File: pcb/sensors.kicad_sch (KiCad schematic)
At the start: 6 parts, among them U3 INA230AIRGTT, U4 MCP9804_DFN, U6 INA230AIRGTT, U7 INA230AIRGTT

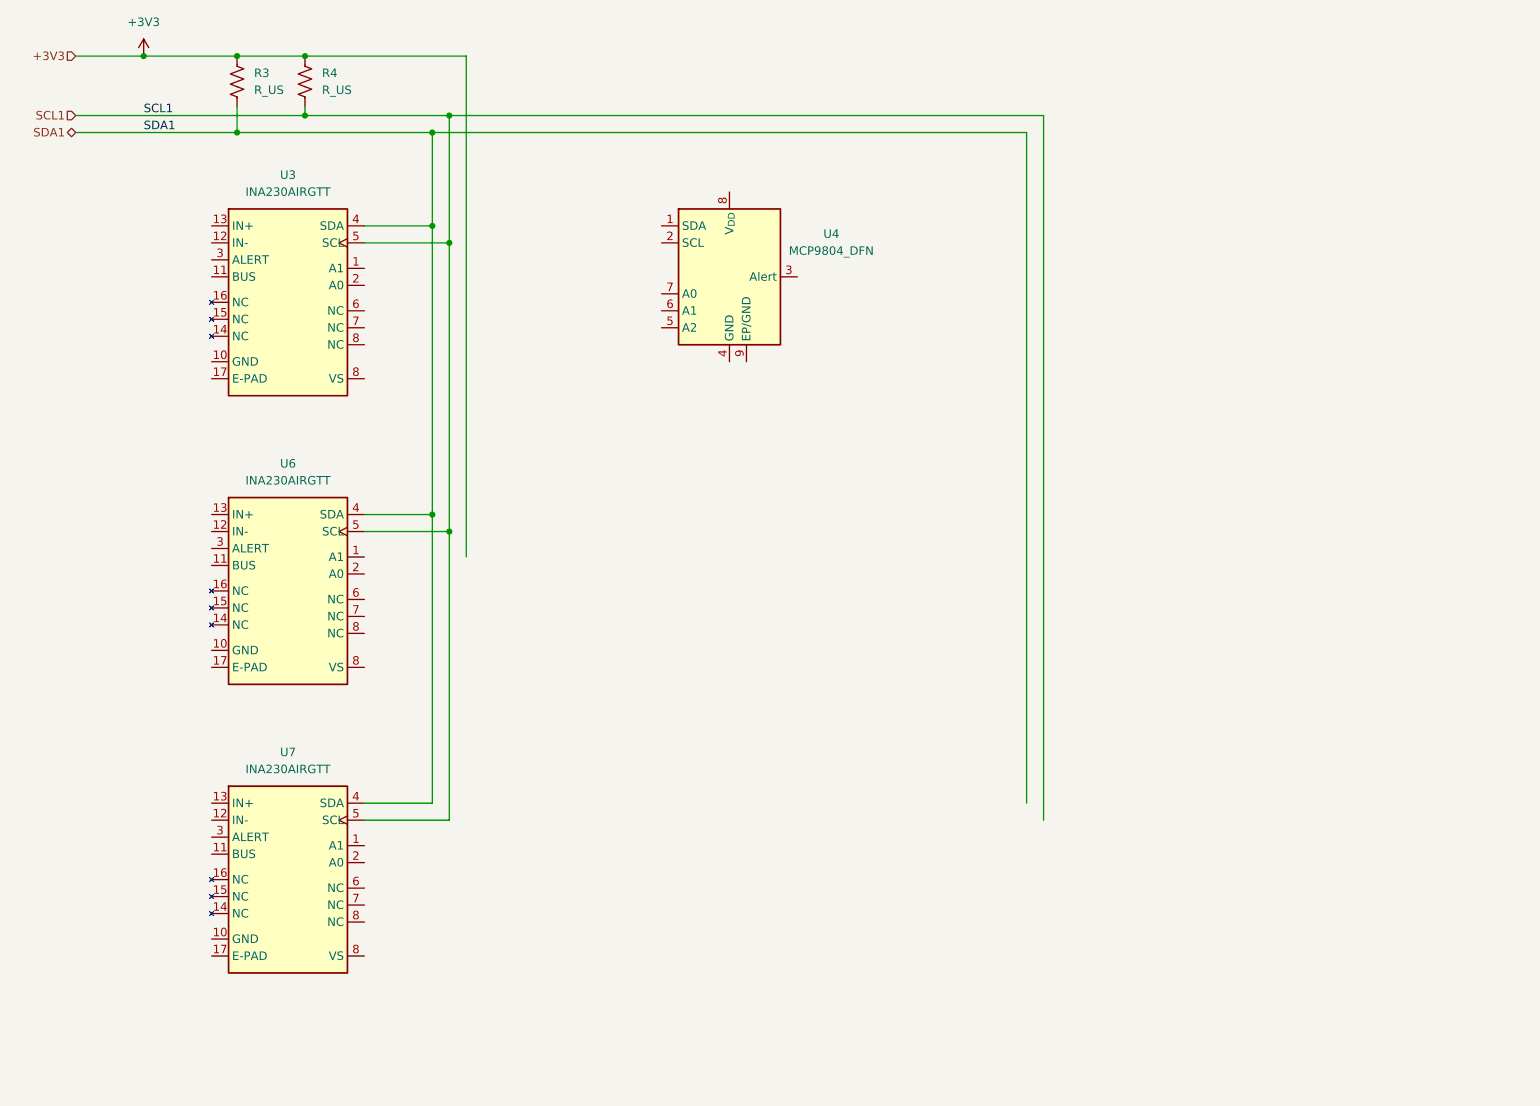
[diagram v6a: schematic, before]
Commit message: completed bus aliasing definitions
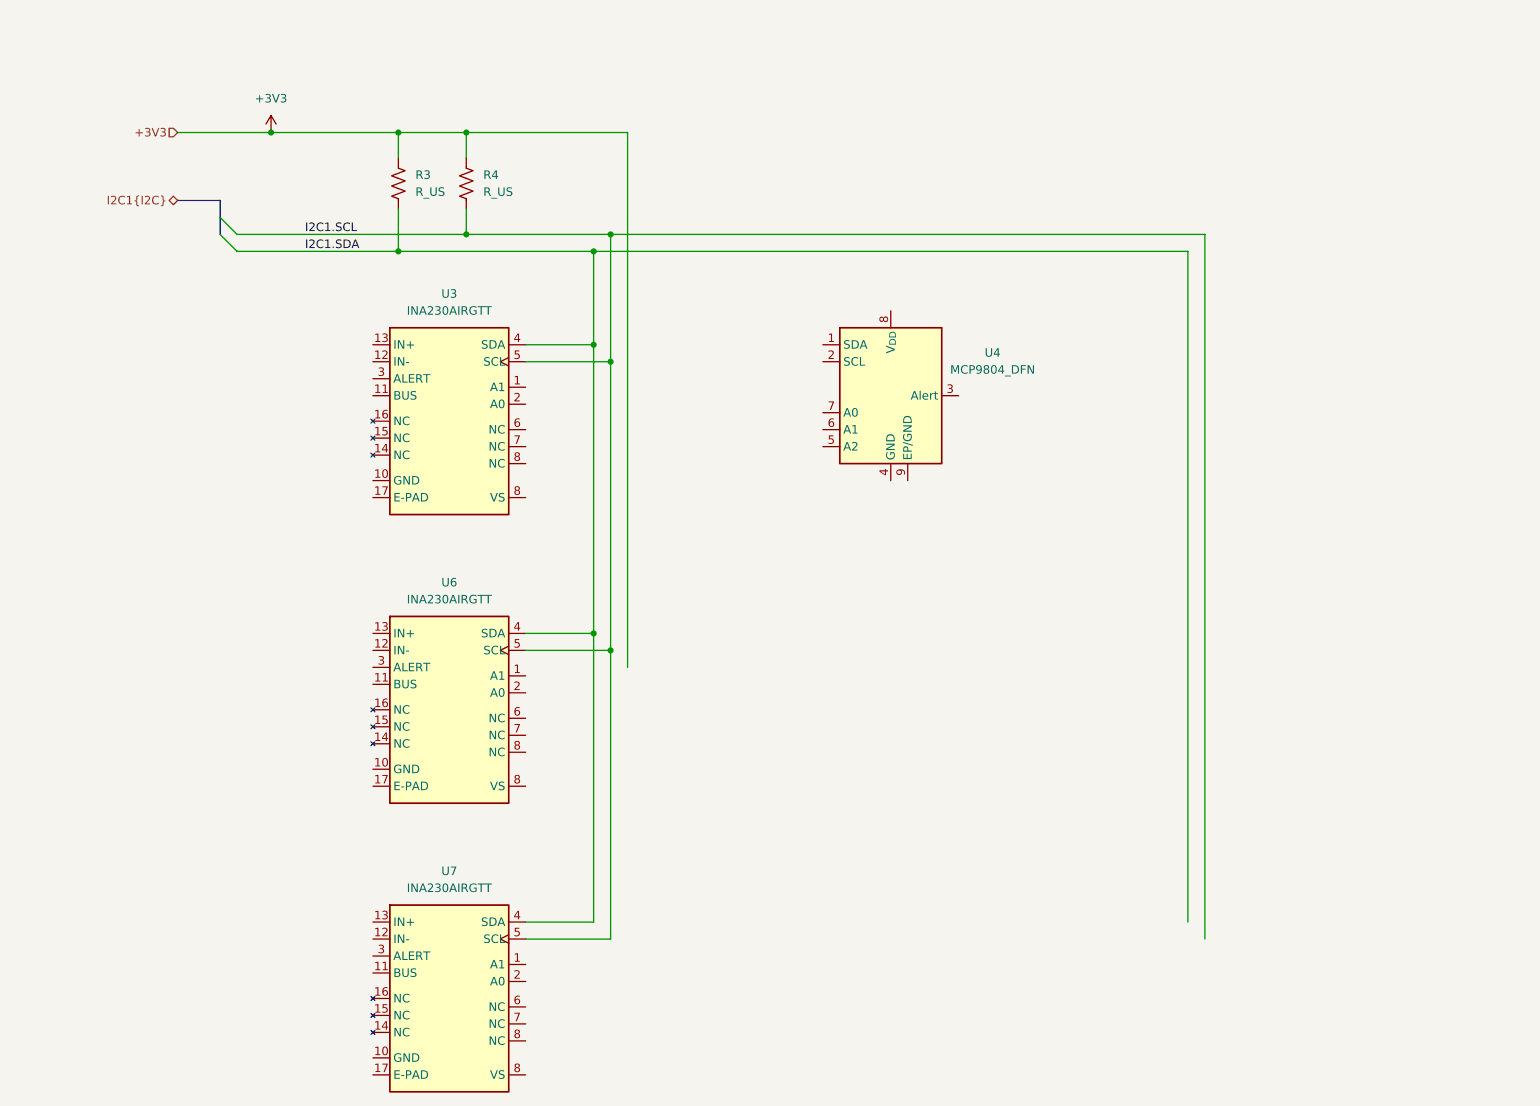
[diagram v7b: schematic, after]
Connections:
- net SCL1 renamed I2C1.SCL
- net SDA1 renamed I2C1.SDA
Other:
- moved on the sheet: R3, R4, U3, U4, U6, U7

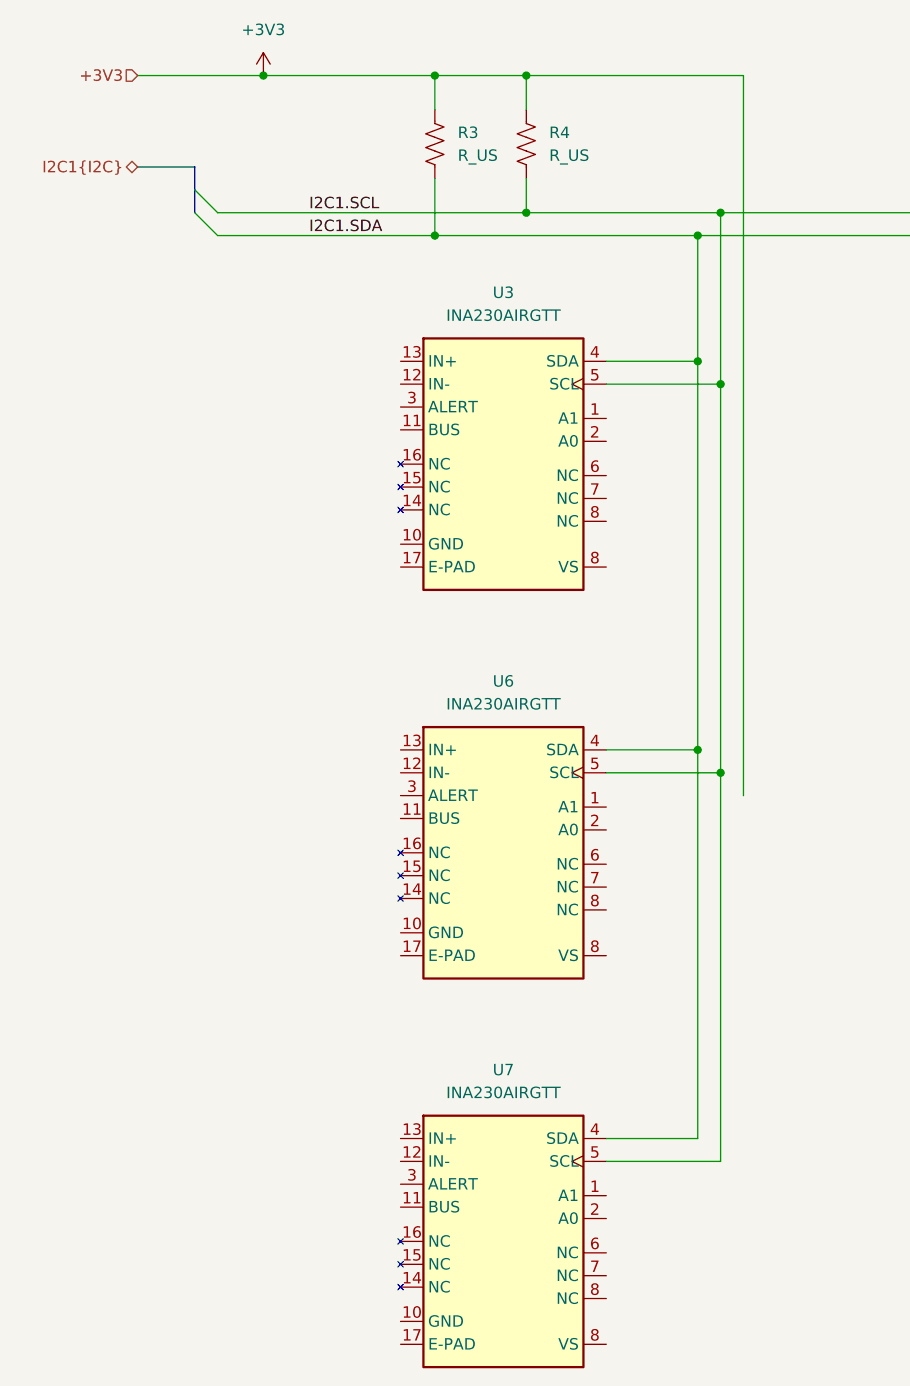
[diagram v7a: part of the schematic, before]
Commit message: updated sims, power hierarchy
added power flags to voltage buses, removed standard kicad "+3.3V" power flags and using standard kicad "power flag" in order to use hierarchical labels to visually show power paths
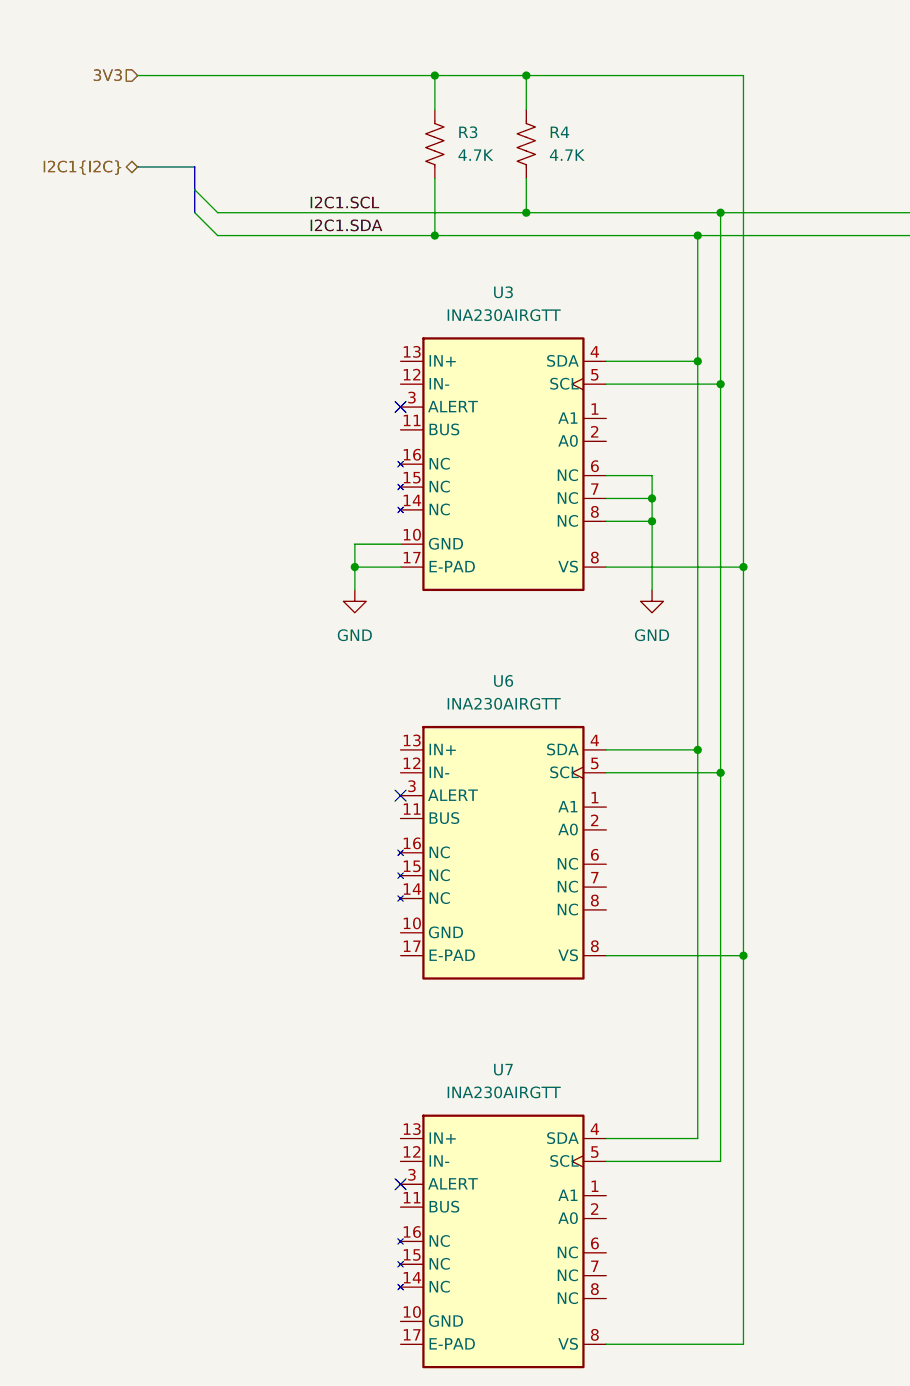
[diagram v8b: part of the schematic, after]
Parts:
- R3, R4: value R_US -> 4.7K; footprint (none) -> Resistor_SMD:R_0402_1005Metric
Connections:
- net +3V3 is gone; now on net 3V3: R3.1, R4.1
- net 3V3: now reaches U7.8 (VS)
- net 3V3: now also U3.8 (VS), U6.8 (VS)
- net GND: now reaches U3.10 (GND)
- net GND: now also U3.17 (E-PAD), U3.6 (NC), U3.7 (NC), U3.8 (VS)
- no-connect marks 0 -> 3
